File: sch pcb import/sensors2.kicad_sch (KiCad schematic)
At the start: 29 parts, among them J501 0734120114, J502 0734120114, J503 Micro_SD_Card, J504 Conn_Coaxial, U501 NEO-6M-GPS, U502 RFM98W-433S2, U503 W25Q128JVS

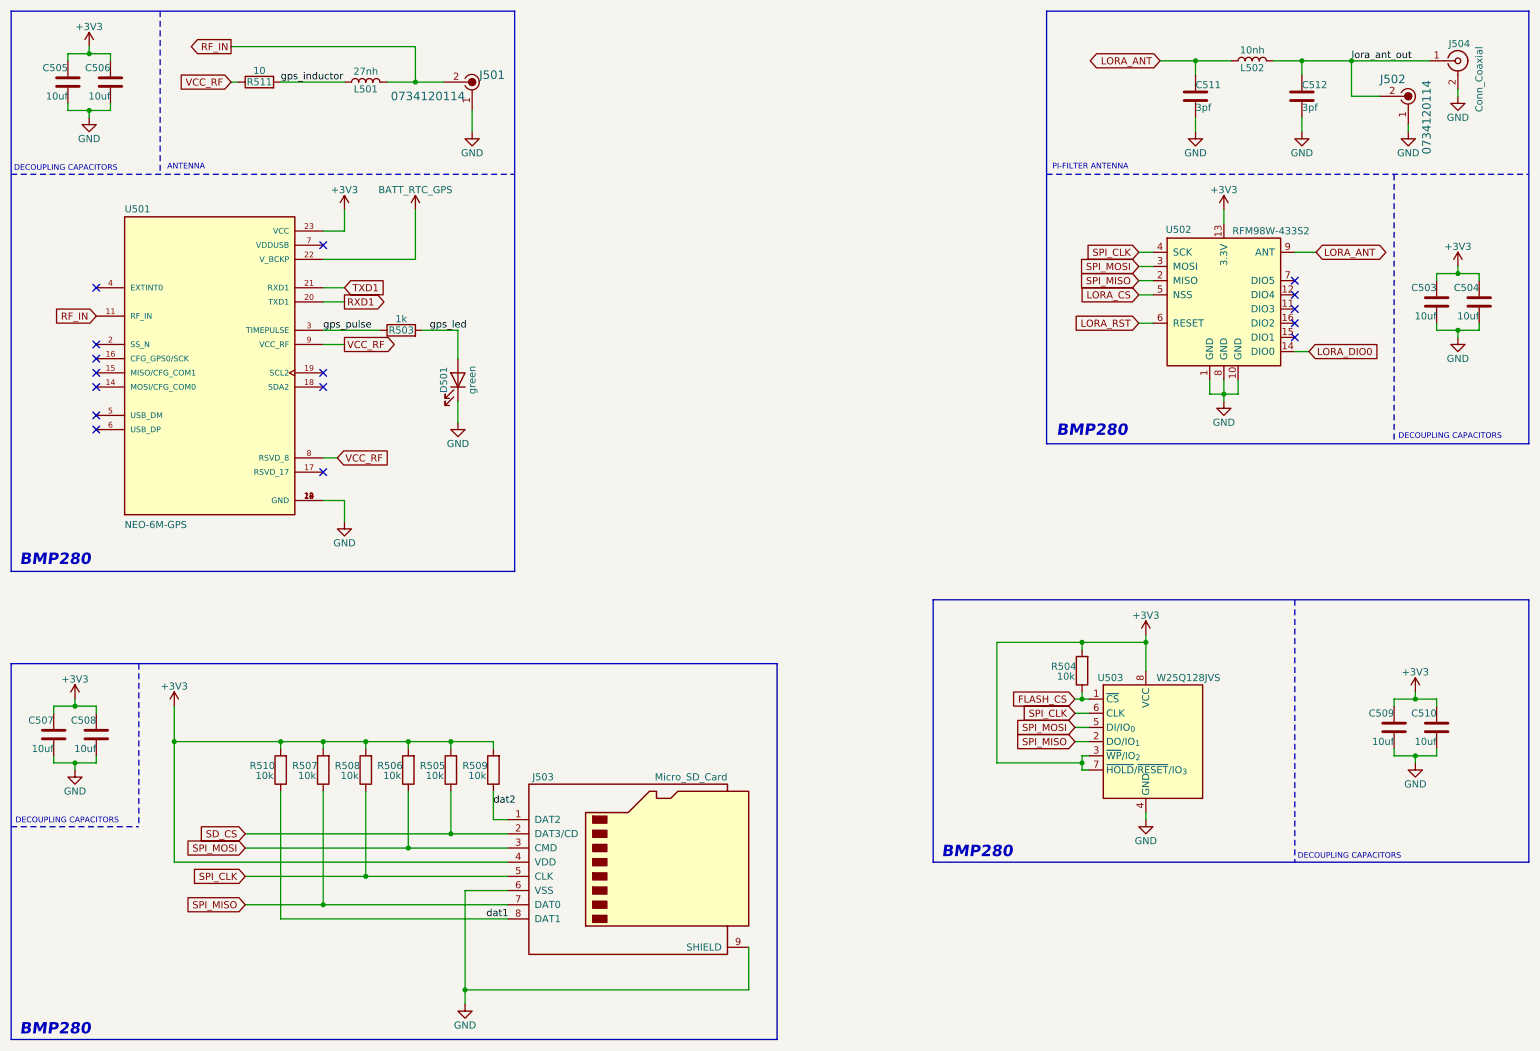
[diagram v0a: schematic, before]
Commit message: added servo and finished esp32 connections
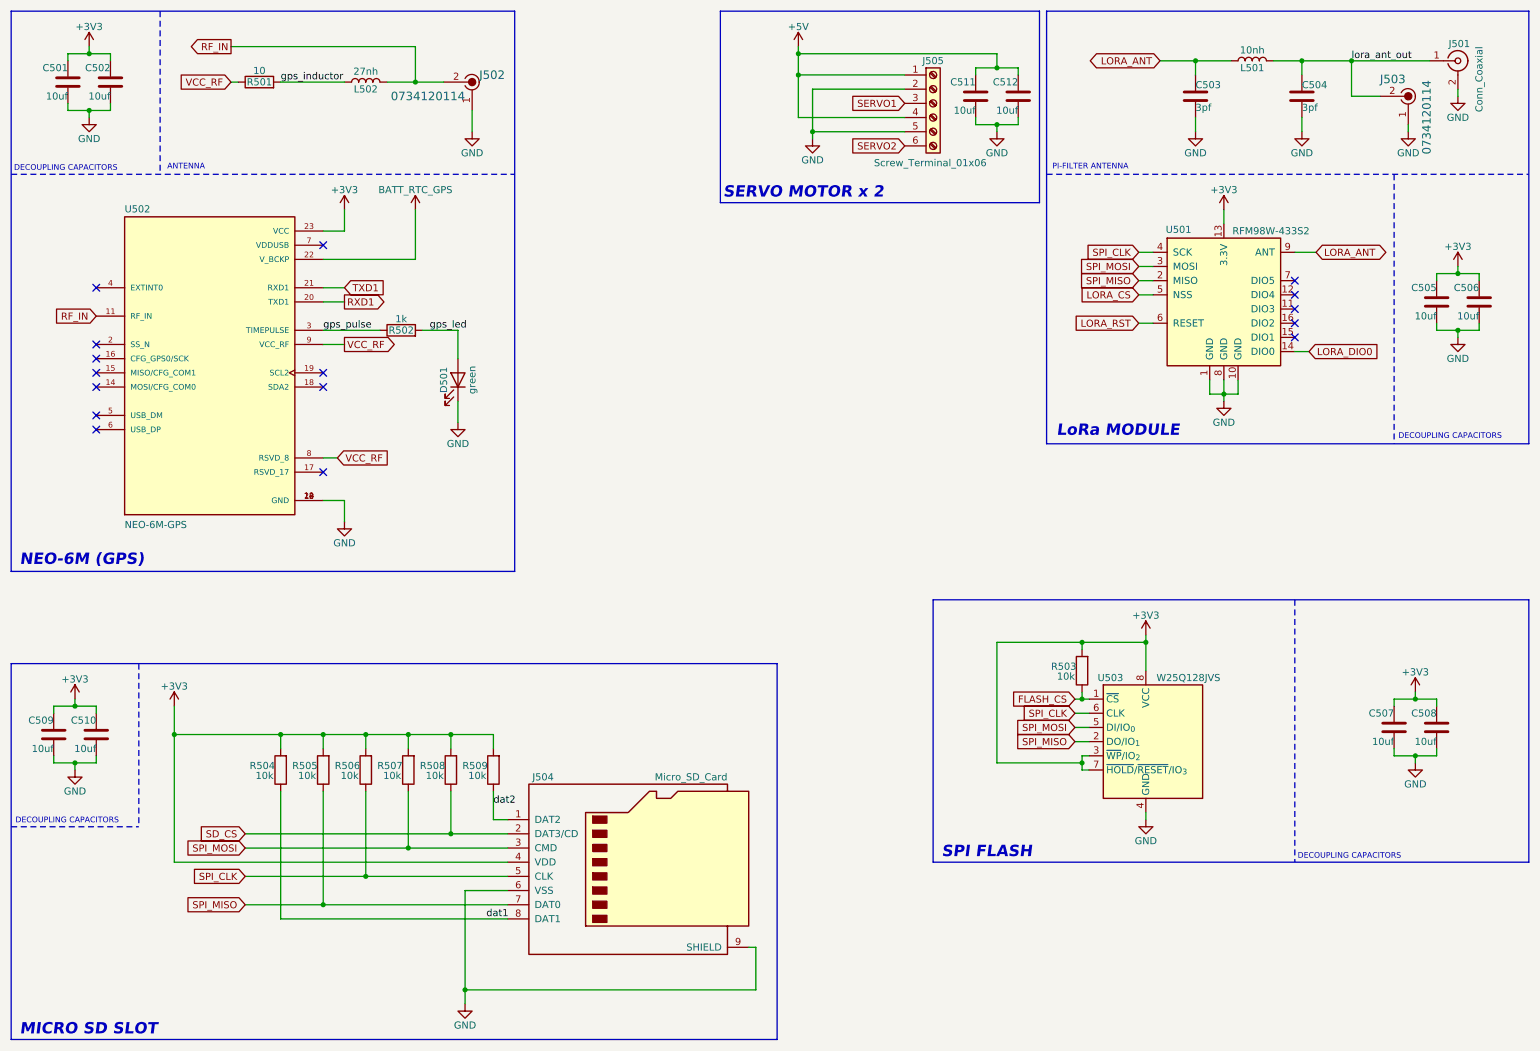
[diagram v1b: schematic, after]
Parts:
- added C511, C512: 10uf, symbol Device:C
- added J505: Screw_Terminal_01x06, TerminalBlock:TerminalBlock_Xinya_XY308-2.54-6P_1x06_P2.54mm_Horizontal, symbol Connector:Screw_Terminal_01x06
- renumbered C505 to C501, C506 to C502, C511 to C503, C512 to C504, C503 to C505, C504 to C506, C509 to C507, C510 to C508, C507 to C509, C508 to C510, J504 to J501, J501 to J502, J502 to J503, J503 to J504, L502 to L501, L501 to L502, R511 to R501, R503 to R502, R504 to R503, R510 to R504, R507 to R505, R508 to R506, R506 to R507, R505 to R508, U502 to U501, U501 to U502
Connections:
- net GND: now also C511.2, C512.2, J505.2 (Pin_2), J505.5 (Pin_5)
- new net +5V: C511.1, C512.1, J505.1 (Pin_1), J505.4 (Pin_4)
- new net SERVO1: J505.3 (Pin_3)
- new net SERVO2: J505.6 (Pin_6)
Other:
- note added: "LoRa MODULE"
- note added: "MICRO SD SLOT"
- note added: "NEO-6M (GPS)"
- note added: "SERVO MOTOR x 2"
- note added: "SPI FLASH"
- note removed: "BMP280"
- company: Done by :- Arudhran -> Drawn by :- Arudhran
- title: AVIONICS PCB -> VECTRON

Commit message: rearranging for aesthetics
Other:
- moved on the sheet: C511, C512, J505

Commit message: minor changes
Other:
- title: VECTRON -> VECTRON-V1
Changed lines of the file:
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@@
 	(paper "A4")
 	(title_block
-		(title "VECTRON")
-		(date "2025-06-10")
+		(title "VECTRON-V1")
+		(date "2025-06-13")
 		(rev "1.0.0")
 		(company "Drawn by :- Arudhran")

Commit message: minor changes
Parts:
- C501, C502, C503, C504, C505, C506, C507, C508, C509, C510, C511, C512: footprint (none) -> Capacitor_SMD:C_0603_1608Metric
- D501: footprint (none) -> LED_SMD:LED_0603_1608Metric
- L501, L502: footprint (none) -> Inductor_SMD:L_0402_1005Metric
- R501, R502, R503, R504, R505, R506, R507, R508, R509: footprint (none) -> Resistor_SMD:R_0603_1608Metric
- U501: footprint (none) -> RF_Module:HOPERF_RFM9XW_SMD
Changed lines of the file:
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@@
 	(text "MICRO SD SLOT\n"
 		(exclude_from_sim no)
-		(at 14.224 195.072 0)
+		(at 13.208 195.072 0)
 		(effects
 			(font
@@
 			)
 		)
-		(property "Footprint" ""
+		(property "Footprint" "Resistor_SMD:R_0603_1608Metric"
 			(at 82.55 71.628 90)
 			(effects
@@
 			)
 		)
-		(property "Footprint" ""
+		(property "Footprint" "Capacitor_SMD:C_0603_1608Metric"
 			(at 23.8252 29.21 0)
 			(effects
@@
 			)
 		)
-		(property "Footprint" ""
+		(property "Footprint" "Capacitor_SMD:C_0603_1608Metric"
 			(at 154.6352 27.94 0)
 			(effects
@@
 			)
 		)
-		(property "Footprint" ""
+		(property "Footprint" "Resistor_SMD:R_0603_1608Metric"
 			(at 77.978 148.59 90)
 			(effects
@@
 			)
 		)
-		(property "Footprint" ""
+		(property "Footprint" "Resistor_SMD:R_0603_1608Metric"
 			(at 70.358 148.59 90)
 			(effects
@@
 			)
 		)
-		(property "Footprint" ""
+		(property "Footprint" "Resistor_SMD:R_0603_1608Metric"
 			(at 100.838 148.59 90)
 			(effects
@@
 			)
 		)
-		(property "Footprint" ""
+		(property "Footprint" "Capacitor_SMD:C_0603_1608Metric"
 			(at 268.9352 144.78 0)
 			(effects
@@
 			)
 		)
-		(property "Footprint" ""
+		(property "Footprint" "RF_Module:HOPERF_RFM9XW_SMD"
 			(at 146.05 21.59 0)
 			(effects
@@
 			)
 		)
-		(property "Footprint" ""
+		(property "Footprint" "Inductor_SMD:L_0402_1005Metric"
 			(at 76.2 25.4 0)
 			(effects
@@
 			)
 		)
-		(property "Footprint" ""
+		(property "Footprint" "Capacitor_SMD:C_0603_1608Metric"
 			(at 147.0152 27.94 0)
 			(effects
@@
 			)
 		)
-		(property "Footprint" ""
+		(property "Footprint" "Resistor_SMD:R_0603_1608Metric"
 			(at 93.218 148.59 90)
 			(effects
@@
 			)
 		)
-		(property "Footprint" ""
+		(property "Footprint" "Capacitor_SMD:C_0603_1608Metric"
 			(at 225.7552 31.75 0)
 			(effects
@@
 			)
 		)
-		(property "Footprint" ""
+		(property "Footprint" "Capacitor_SMD:C_0603_1608Metric"
 			(at 21.2852 146.05 0)
 			(effects
@@
 			)
 		)
-		(property "Footprint" ""
+		(property "Footprint" "Resistor_SMD:R_0603_1608Metric"
 			(at 206.248 130.81 90)
 			(effects
@@
 			)
 		)
-		(property "Footprint" ""
+		(property "Footprint" "Resistor_SMD:R_0603_1608Metric"
 			(at 62.738 148.59 90)
 			(effects
@@
 			)
 		)
-		(property "Footprint" ""
+		(property "Footprint" "Inductor_SMD:L_0402_1005Metric"
 			(at 234.95 21.59 0)
 			(effects
@@
 			)
 		)
-		(property "Footprint" ""
+		(property "Footprint" "Capacitor_SMD:C_0603_1608Metric"
 			(at 31.4452 29.21 0)
 			(effects
@@
 			)
 		)
-		(property "Footprint" ""
+		(property "Footprint" "Resistor_SMD:R_0603_1608Metric"
 			(at 85.598 148.59 90)
 			(effects
@@
 			)
 		)
-		(property "Footprint" ""
+		(property "Footprint" "Resistor_SMD:R_0603_1608Metric"
 			(at 57.15 27.178 90)
 			(effects
@@
 			)
 		)
-		(property "Footprint" ""
+		(property "Footprint" "Capacitor_SMD:C_0603_1608Metric"
 			(at 268.9352 68.58 0)
 			(effects
@@
 			)
 		)
-		(property "Footprint" ""
+		(property "Footprint" "Capacitor_SMD:C_0603_1608Metric"
 			(at 276.5552 68.58 0)
 			(effects
@@
 			)
 		)
-		(property "Footprint" ""
+		(property "Footprint" "Capacitor_SMD:C_0603_1608Metric"
 			(at 28.9052 146.05 0)
 			(effects
@@
 			)
 		)
-		(property "Footprint" ""
+		(property "Footprint" "Capacitor_SMD:C_0603_1608Metric"
 			(at 261.3152 144.78 0)
 			(effects
@@
 			)
 		)
-		(property "Footprint" ""
+		(property "Footprint" "Capacitor_SMD:C_0603_1608Metric"
 			(at 244.8052 31.75 0)
 			(effects
@@
 			)
 		)
-		(property "Footprint" ""
+		(property "Footprint" "LED_SMD:LED_0603_1608Metric"
 			(at 92.71 78.74 0)
 			(effects

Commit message: minor changes
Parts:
- renumbered C511 to C501, C512 to C502, C501 to C503, C502 to C504, C503 to C505, C504 to C506, C505 to C507, C506 to C508, C507 to C509, C508 to C510, C509 to C511, C510 to C512, J505 to J504, J504 to J505

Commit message: minor changes
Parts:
- removed C501, C502: 10uf, Capacitor_SMD:C_0603_1608Metric, symbol Device:C
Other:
- company: Drawn by :- Arudhran -> (none)
- moved on the sheet: J504
